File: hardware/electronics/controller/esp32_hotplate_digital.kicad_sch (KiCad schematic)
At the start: 92 parts, among them IC1 ADC081S021CIMF_NOPB, IC2 ADC081S021CIMF_NOPB, J1 USB_C_Receptacle_USB2.0, J2 JST XH, J3 JST XH, J4 JST XH, J5 JST XH, J7 JST XH, J8 105162-0001, J9 Conn_01x04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

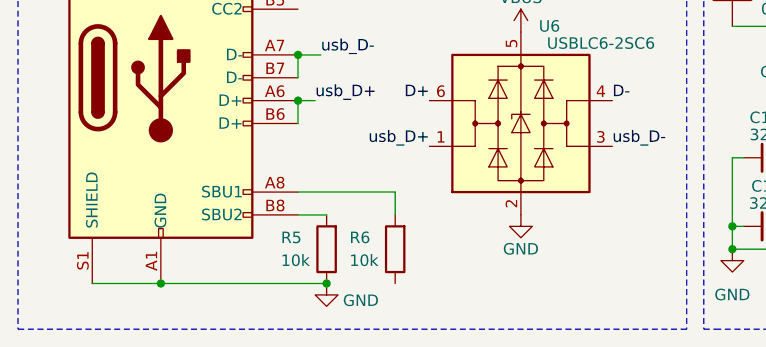
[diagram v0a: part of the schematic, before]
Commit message: controller can now draw reflow profiles from the sd card, if no card is available a default profile will be loaded
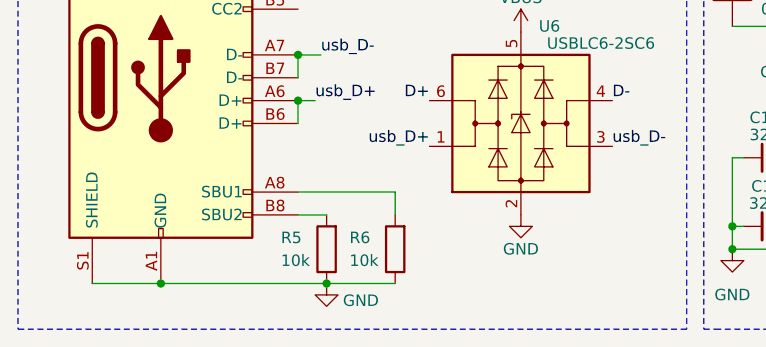
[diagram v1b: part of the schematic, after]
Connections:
- net GND: now also R6.1
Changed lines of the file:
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@@
+    (stroke (width 0) (type default))
+  )
+  (wire (pts (xy 48.895 185.42) (xy 56.515 185.42))
     (stroke (width 0) (type default))
   )

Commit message: finalized the controller version 2
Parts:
- added D10, D5: LED, LED_SMD:LED_0805_2012Metric_Pad1.15x1.40mm_HandSolder, symbol Device:LED
- added R28, R29: 10k, Resistor_SMD:R_0805_2012Metric_Pad1.20x1.40mm_HandSolder, symbol Device:R
- R20, R7, R8: value R -> 10k
- R5, R6: value 10k -> 5.1k
- R9: value R -> 4k7
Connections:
- net FAN: now also R28.1
- net GND: now also D10.1 (K), D5.1 (K)
- net HEATER: now also R29.1
- new net: D10.2 (A), R29.2
- new net: D5.2 (A), R28.2
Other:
- moved on the sheet: F2

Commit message: updated code + added 3d pintable parts + added thermal isolation pcb
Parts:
- added C22: 0.1uf, Capacitor_SMD:C_0603_1608Metric_Pad1.08x0.95mm_HandSolder, symbol Device:C_Small
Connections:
- net +3.3V: now also C22.1
- net GND: now also C22.2
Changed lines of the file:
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@@
+    )
+  )
+  (symbol (lib_id "power:+3.3V") (at 148.59 150.495 0) (unit 1)
+    (in_bom yes) (on_board yes) (dnp no)
+    (property "Reference" "#PWR011" (at 148.59 154.305 0)
+      (effects (font (size 1.27 1.27)) hide)
+    )
+    (property "Value" "+3.3V" (at 152.4 148.59 0)
+      (effects (font (size 1.27 1.27)))
+    )
+    (property "Footprint" "" (at 148.59 150.495 0)
+      (effects (font (size 1.27 1.27)) hide)
+    )
+    (property "Datasheet" "" (at 148.59 150.495 0)
+      (effects (font (size 1.27 1.27)) hide)
+    )
+    (pin "1")
+    (instances
+      (project "esp32_hotplate_digital"
+        (path "/9f056549-b338-4bd0-9690-14155344f3fa"
+          (reference "#PWR011") (unit 1)
+        )
+      )
     )
   )
@@
     )
   )
+  (symbol (lib_id "power:GND") (at 148.59 155.575 0) (unit 1)
+    (in_bom yes) (on_board yes) (dnp no)
+    (property "Reference" "#PWR012" (at 148.59 161.925 0)
+      (effects (font (size 1.27 1.27)) hide)
+    )
+    (property "Value" "GND" (at 152.4 157.48 0)
+      (effects (font (size 1.27 1.27)))
+    )
+    (property "Footprint" "" (at 148.59 155.575 0)
+      (effects (font (size 1.27 1.27)) hide)
+    )
+    (property "Datasheet" "" (at 148.59 155.575 0)
+      (effects (font (size 1.27 1.27)) hide)
+    )
+    (pin "1")
+    (instances
+      (project "esp32_hotplate_digital"
+        (path "/9f056549-b338-4bd0-9690-14155344f3fa"
+          (reference "#PWR012") (unit 1)
+        )
+      )
+    )
+  )
   (symbol (lib_id "power:+3.3V") (at 36.83 24.13 0) (unit 1)
     (in_bom yes) (on_board yes) (dnp no) (fields_autoplaced)
@@
         )
       )
+    )
+  )
+  (symbol (lib_id "Device:C_Small") (at 148.59 153.035 0) (mirror y) (unit 1)
+    (in_bom yes) (on_board yes) (dnp no)
+    (property "Reference" "C22" (at 150.495 152.4 0)
+      (effects (font (size 1.27 1.27)) (justify right))
+    )
+    (property "Value" "0.1uf" (at 150.495 154.305 0)
+      (effects (font (size 1.27 1.27)) (justify right))
+    )
+    (property "Footprint" "Capacitor_SMD:C_0603_1608Metric_Pad1.08x0.95mm_HandSolder" (at 148.59 153.035 0)
+      (effects (font (size 1.27 1.27)) hide)
+    )
+    (property "Datasheet" "~" (at 148.59 153.035 0)
+      (effects (font (size 1.27 1.27)) hide)
+    )
+    (pin "1")
+    (pin "2")
+    (instances
+      (project "esp32_hotplate_digital"
+        (path "/9f056549-b338-4bd0-9690-14155344f3fa"
+          (reference "C22") (unit 1)
+        )
+      )
+      (project "ssd2828_board"
+        (path "/e63e39d7-6ac0-4ffd-8aa3-1841a4541b55"
+          (reference "C1") (unit 1)
+        )
+      )
